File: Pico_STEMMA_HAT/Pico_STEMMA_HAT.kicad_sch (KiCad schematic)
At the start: 38 parts, among them J1 Conn_01x20_Socket, J2 Conn_01x20_Socket

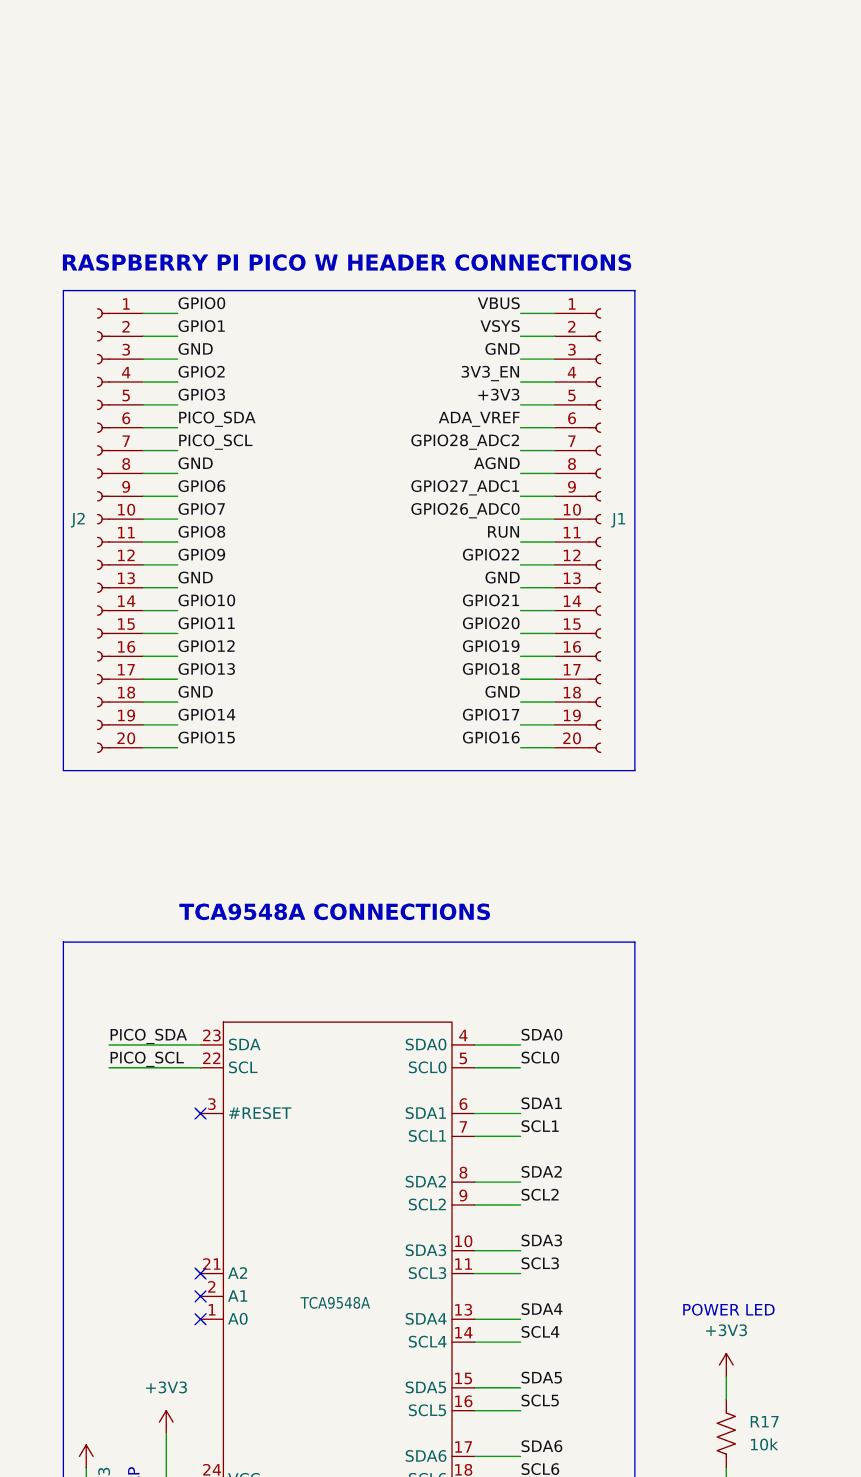
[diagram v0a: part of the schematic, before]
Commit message: Add STEMMA connector pads to the GND net
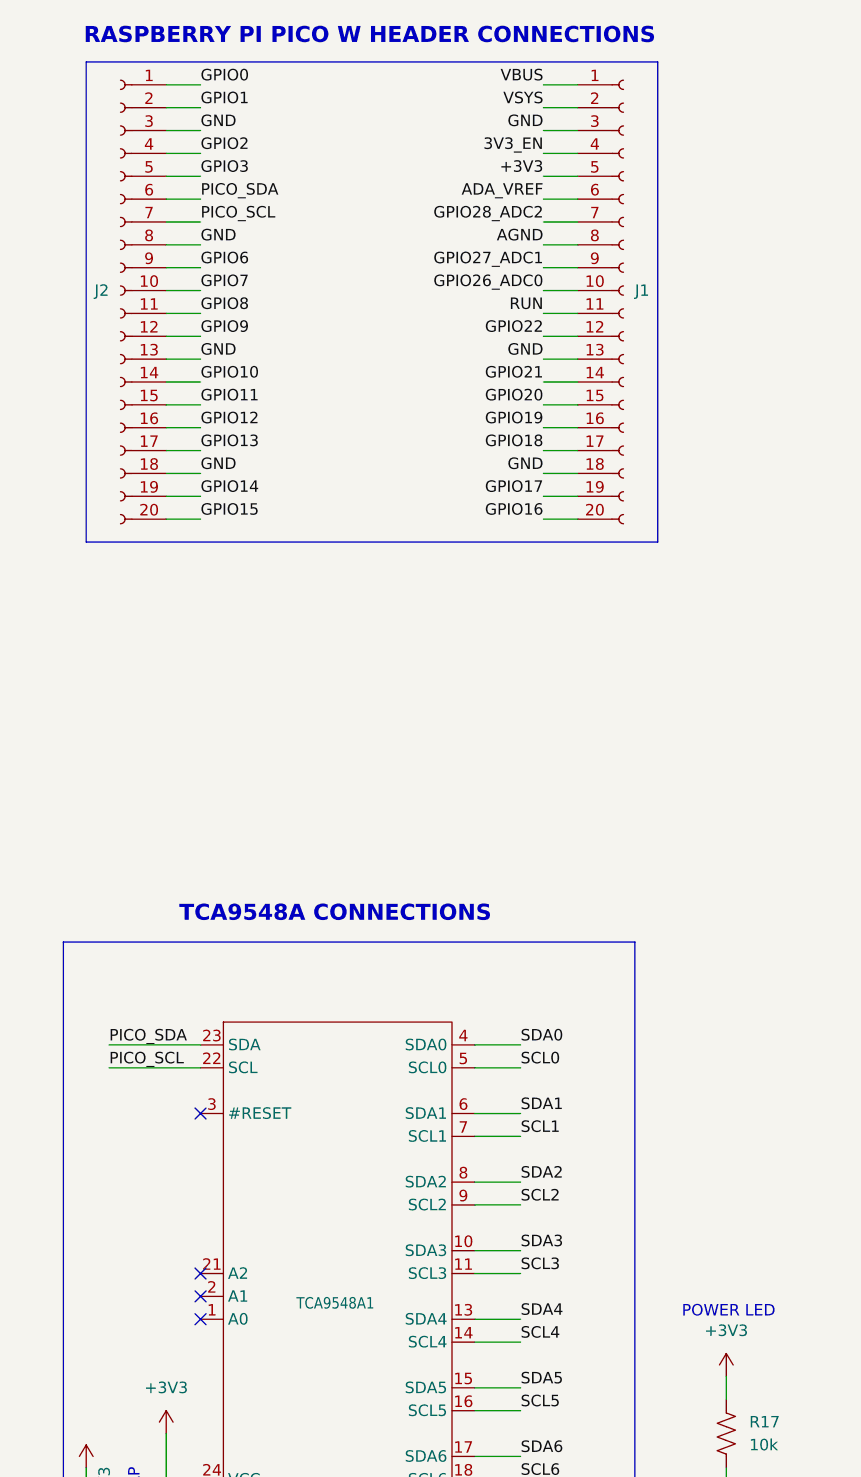
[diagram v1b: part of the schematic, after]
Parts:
- renumbered TCA9548A to TCA9548A1
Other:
- moved on the sheet: J1, J2

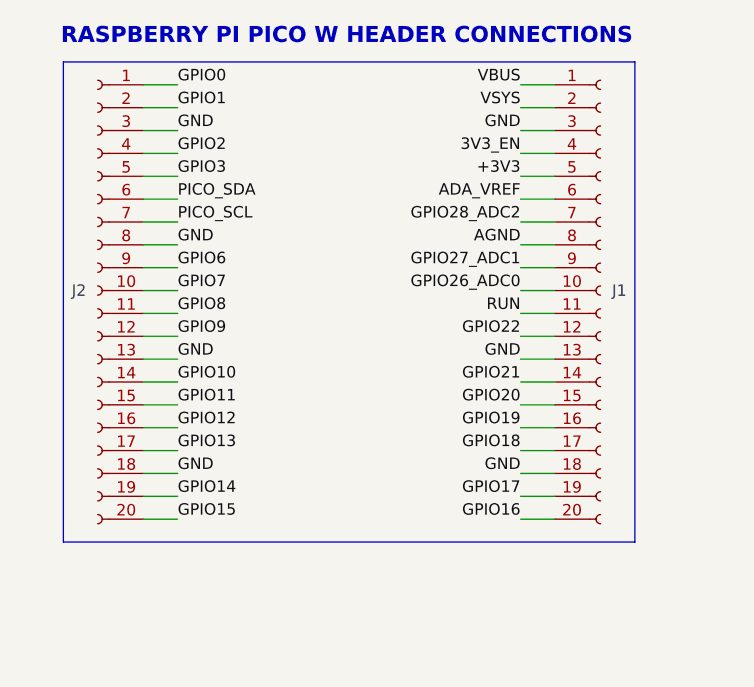
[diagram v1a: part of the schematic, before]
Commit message: Fix errors from the DRC
The design rules are based around the JLCPCB manufacturer
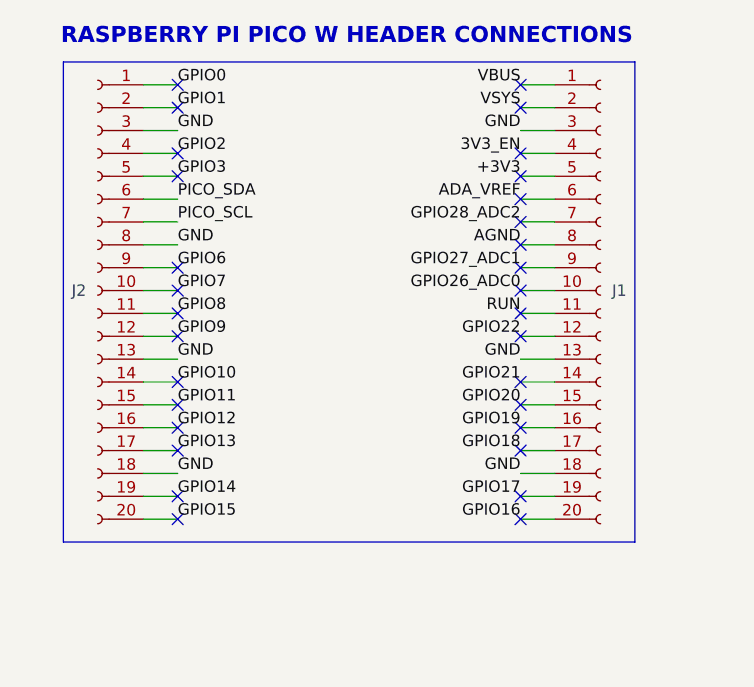
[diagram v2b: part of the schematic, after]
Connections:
- no-connect marks 4 -> 35
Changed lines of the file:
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@@
+	)
+	(no_connect
+		(at 27.94 53.34)
+	)
+	(no_connect
+		(at 27.94 40.64)
 	)
 	(no_connect
@@
 	)
 	(no_connect
+		(at 66.04 17.78)
+	)
+	(no_connect
+		(at 66.04 43.18)
+	)
+	(no_connect
+		(at 27.94 45.72)
+	)
+	(no_connect
+		(at 66.04 35.56)
+	)
+	(no_connect
+		(at 27.94 43.18)
+	)
+	(no_connect
+		(at 66.04 40.64)
+	)
+	(no_connect
+		(at 27.94 55.88)
+	)
+	(no_connect
+		(at 27.94 50.8)
+	)
+	(no_connect
+		(at 66.04 33.02)
+	)
+	(no_connect
+		(at 27.94 17.78)
+	)
+	(no_connect
+		(at 66.04 58.42)
+	)
+	(no_connect
+		(at 27.94 25.4)
+	)
+	(no_connect
+		(at 66.04 63.5)
+	)
+	(no_connect
+		(at 66.04 20.32)
+	)
+	(no_connect
 		(at 27.94 154.94)
+	)
+	(no_connect
+		(at 66.04 38.1)
+	)
+	(no_connect
+		(at 66.04 25.4)
+	)
+	(no_connect
+		(at 27.94 27.94)
 	)
 	(no_connect
@@
 	)
 	(no_connect
+		(at 27.94 38.1)
+	)
+	(no_connect
+		(at 66.04 53.34)
+	)
+	(no_connect
+		(at 27.94 58.42)
+	)
+	(no_connect
+		(at 66.04 45.72)
+	)
+	(no_connect
+		(at 27.94 20.32)
+	)
+	(no_connect
+		(at 27.94 66.04)
+	)
+	(no_connect
 		(at 27.94 132.08)
 	)
+	(no_connect
+		(at 27.94 63.5)
+	)
+	(no_connect
+		(at 66.04 55.88)
+	)
+	(no_connect
+		(at 66.04 27.94)
+	)
+	(no_connect
+		(at 66.04 30.48)
+	)
+	(no_connect
+		(at 66.04 66.04)
+	)
+	(no_connect
+		(at 66.04 50.8)
+	)
 	(wire

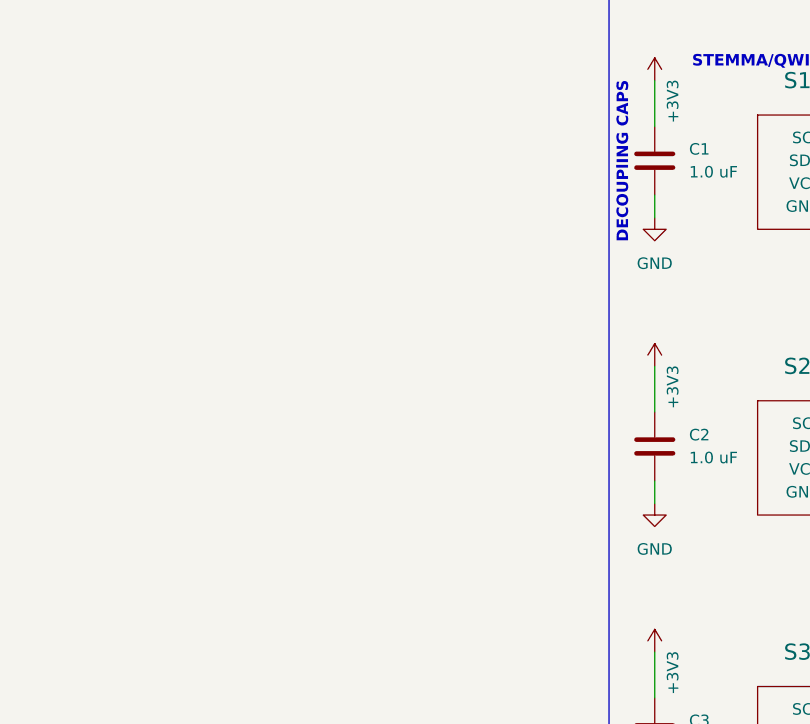
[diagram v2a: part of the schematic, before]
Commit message: Fix 3D model rendering in MacOS
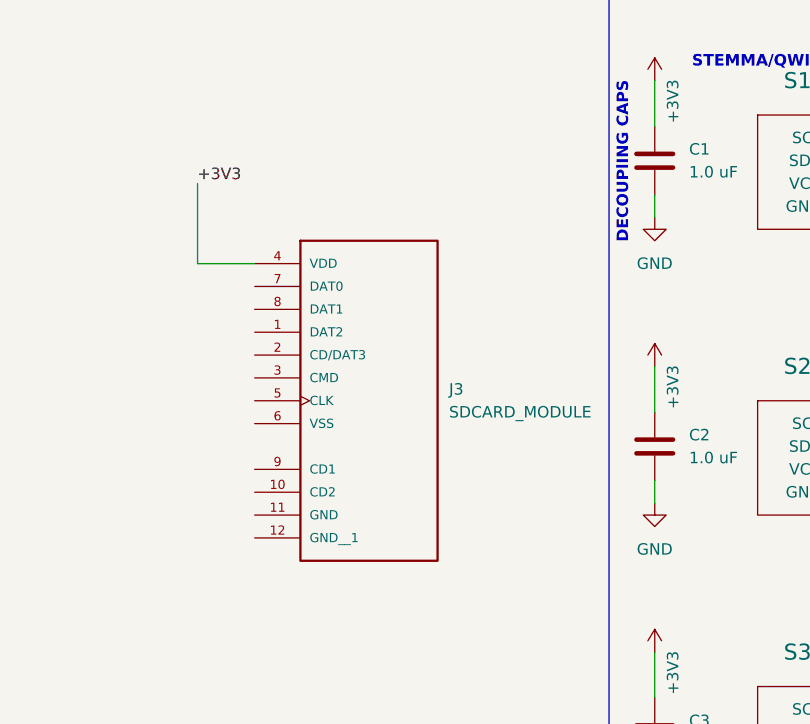
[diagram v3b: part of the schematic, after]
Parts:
- added J3: SDCARD_MODULE, Pico_Footprints:SDCARD_MODULE_Footprint, symbol Pico_Symbols:SDCARD_MODULE
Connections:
- net +3V3: now also J3.4 (VDD)
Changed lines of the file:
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@@
 	(wire
 		(pts
+			(xy 118.11 57.15) (xy 118.11 66.04)
+		)
+		(stroke
+			(width 0)
+			(type default)
+		)
+	)
+	(wire
+		(pts
 			(xy 193.04 154.94) (xy 196.85 154.94)
 		)
@@
 	(wire
 		(pts
+			(xy 118.11 66.04) (xy 124.46 66.04)
+		)
+		(stroke
+			(width 0)
+			(type default)
+		)
+	)
+	(wire
+		(pts
 			(xy 271.78 81.28) (xy 271.78 86.36)
 		)
@@
 		)
 	)
+	(label "+3V3"
+		(at 118.11 57.15 0)
+		(fields_autoplaced yes)
+		(effects
+			(font
+				(size 1.27 1.27)
+			)
+			(justify left bottom)
+		)
+	)
 	(label "SDA4"
 		(at 278.13 54.61 0)
@@
 					(unit 1)
 				)
+			)
+		)
+	)
+	(symbol
+		(lib_id "Pico_Symbols:SDCARD_MODULE")
+		(at 129.54 78.74 0)
+		(unit 1)
+		(exclude_from_sim no)
+		(in_bom yes)
+		(on_board yes)
+		(dnp no)
+		(fields_autoplaced yes)
+		(property "Reference" "J3"
+			(at 146.05 80.0099 0)
+			(effects
+				(font
+					(size 1.27 1.27)
+				)
+				(justify left)
+			)
+		)
+		(property "Value" "SDCARD_MODULE"
+			(at 146.05 82.5499 0)
+			(effects
+				(font
+					(size 1.27 1.27)
+				)
+				(justify left)
+			)
+		)
+		(property "Footprint" "Pico_Footprints:SDCARD_MODULE_Footprint"
+			(at 137.16 61.722 0)
+			(effects
+				(font
+					(size 1.27 1.27)
+				)
+				(justify bottom)
+				(hide yes)
+			)
+		)
+		(property "Datasheet" ""
+			(at 129.54 78.74 0)
+			(effects
+				(font
+					(size 1.27 1.27)
+				)
+				(hide yes)
+			)
+		)
+		(property "Description" ""
+			(at 129.54 78.74 0)
+			(effects
+				(font
+					(size 1.27 1.27)
+				)
+				(hide yes)
+			)
+		)
+		(property "MANUFACTURER" "GCT"
+			(at 129.54 78.74 0)
+			(effects
+				(font
+					(size 1.27 1.27)
+				)
+				(justify bottom)
+				(hide yes)
+			)
+		)
+		(pin "5"
+		)
+		(pin "1"
+		)
+		(pin "7"
+		)
+		(pin "10"
+		)
+		(pin "11"
+		)
+		(pin "4"
+		)
+		(pin "6"
+		)
+		(pin "9"
+		)
+		(pin "2"
+		)
+		(pin "12"
+		)
+		(pin "8"
+		)
+		(pin "3"
+		)
+		(instances
+			(project ""
+				(path "/d7f0761f-a3d3-4a87-8eca-6574a8f4791b"
+					(reference "J3")
+					(unit 1)
+				)

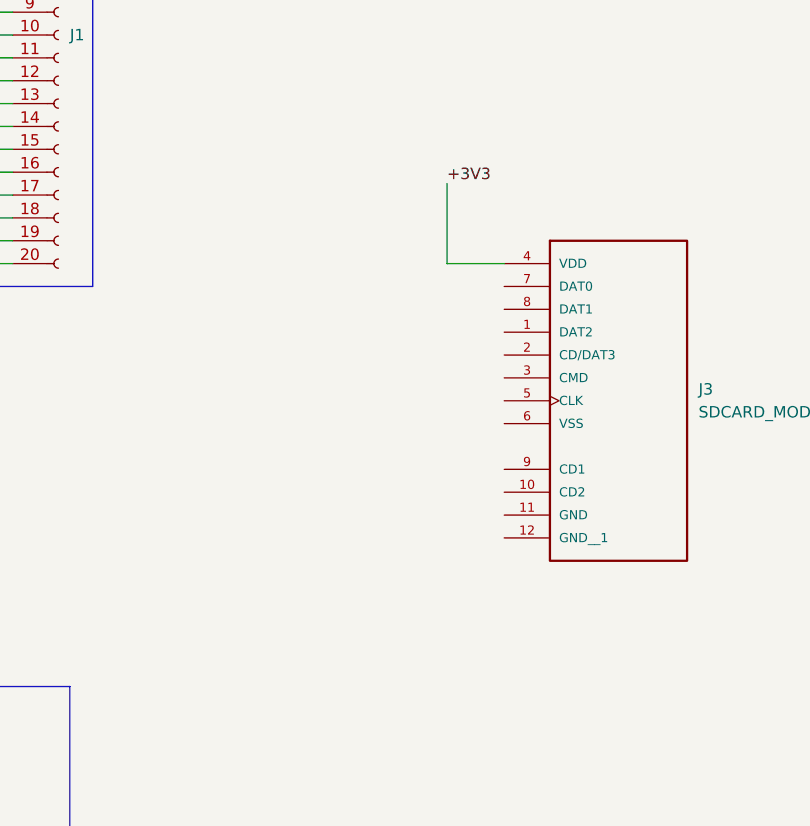
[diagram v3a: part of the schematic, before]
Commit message: Add SD Card reader to schem
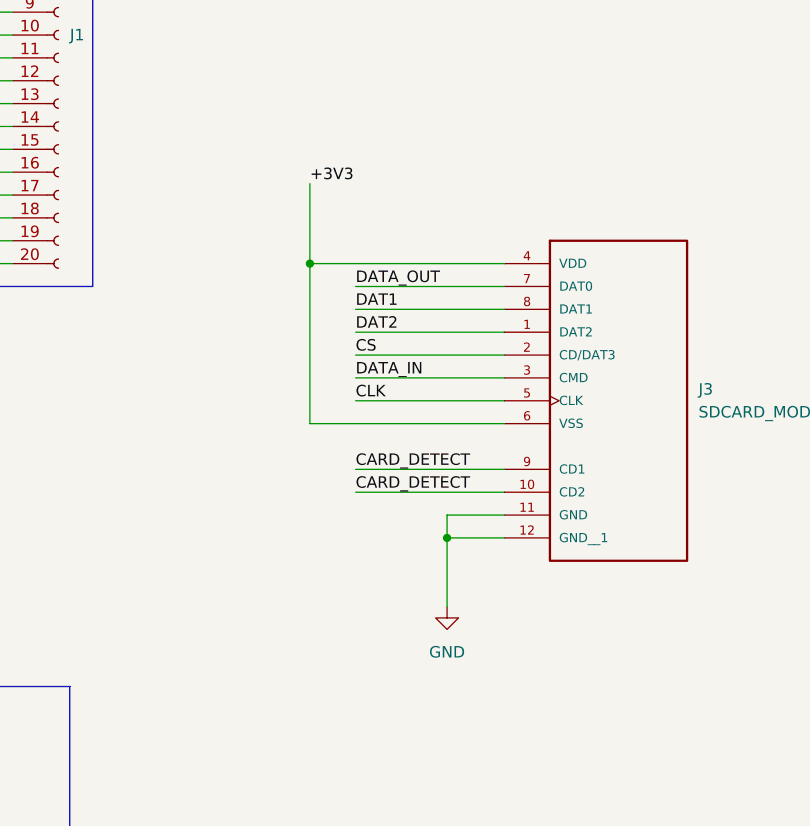
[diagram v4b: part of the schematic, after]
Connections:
- net +3V3: now also J3.6 (VSS)
- net GND: now also J3.11 (GND), J3.12 (GND__1)
- net DAT2: now reaches J3.1 (DAT2)
- net CARD_DETECT: now reaches J3.10 (CD2)
- net CARD_DETECT: now also J3.9 (CD1)
- net CS: now reaches J3.2 (CD/DAT3)
- net DATA_IN: now reaches J3.3 (CMD)
- net CLK: now reaches J3.5 (CLK)
- net DATA_OUT: now reaches J3.7 (DAT0)
- net DAT1: now reaches J3.8 (DAT1)
